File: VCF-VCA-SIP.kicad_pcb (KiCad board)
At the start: 2 copper layers, 40 x 18 mm, 44 parts, among them P1 CONN_10, Q1 BC857BS, U1 LM13700, U2 TL074-, U3 LM13700, U4 LM13700, U5 TL072-

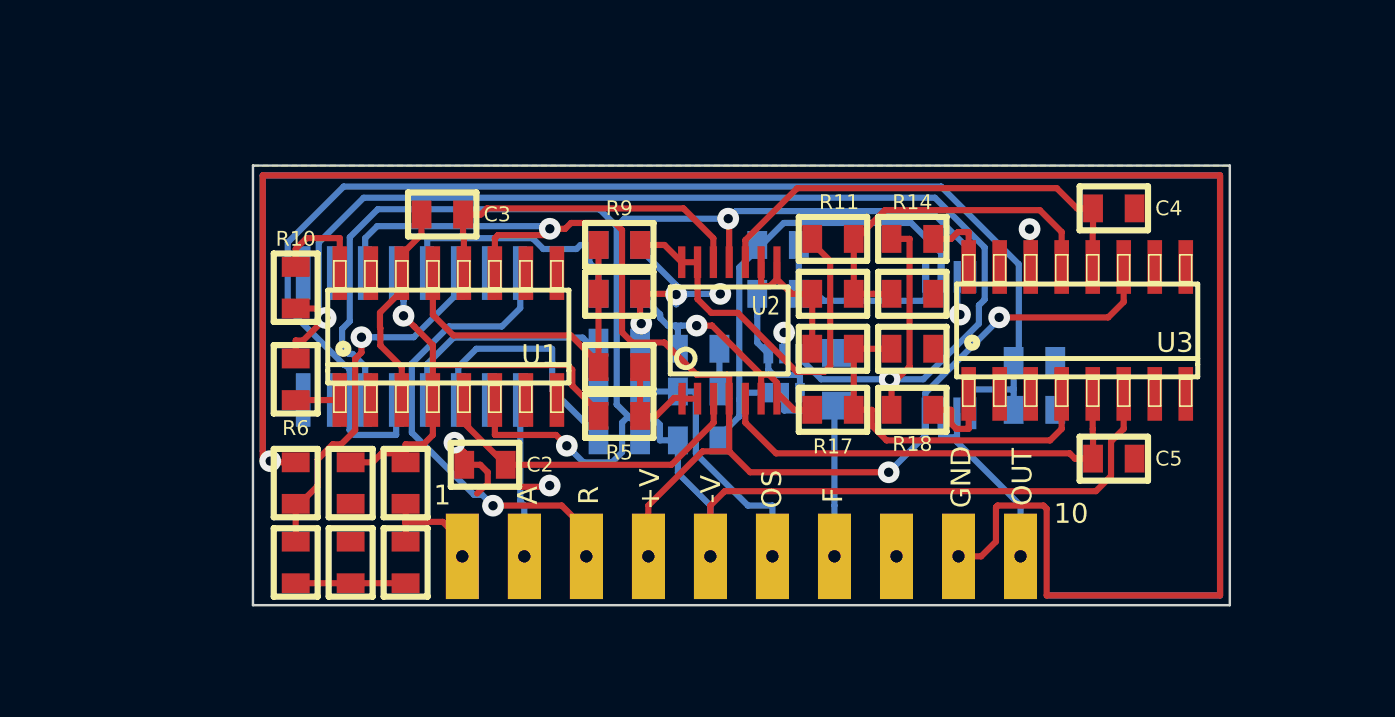
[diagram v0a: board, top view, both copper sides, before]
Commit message: starting to reroute board so trace bewteen LM13700 output in VCA is close to non-inverting input of TL072
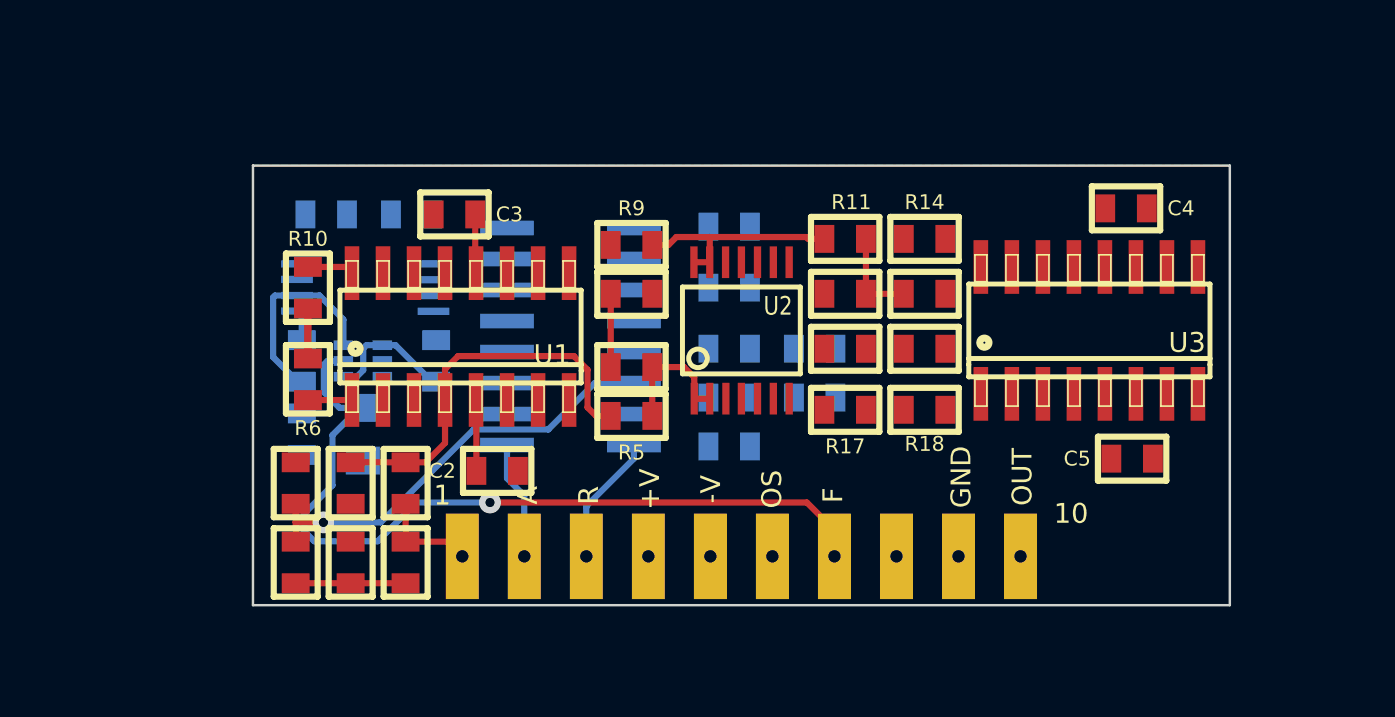
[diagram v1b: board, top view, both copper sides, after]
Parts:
- moved C6 30.1 mm to (101.0, 85.0), turned to 180 degrees
- moved R26 26.2 mm to (104.5, 85.0)
- moved U5 24.1 mm to (102.5, 88.0), turned to 90 degrees
- moved C1 20.1 mm to (100.0, 91.0), turned to 270 degrees
- moved R29 19.6 mm to (102.5, 94.0), turned to 270 degrees
- moved Q1 17.3 mm to (102.5, 91.0), turned to 270 degrees
- moved R1 16.3 mm to (100.0, 94.0), turned to 270 degrees
- moved R2 14.3 mm to (105.5, 91.0), turned to 90 degrees
- moved U4 6.50 mm to (111.0, 90.0), turned to 90 degrees
- moved R30 4.76 mm to (121.0, 92.5)
- moved C7 4.75 mm to (121.0, 90.5)
- moved R22 4.56 mm to (117.5, 85.5)
- moved R20 4.51 mm to (117.5, 88.0)
- moved R23 4.51 mm to (117.5, 92.5)
- moved R24 4.51 mm to (117.5, 90.5)
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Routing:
- net GND: track 188.2 -> 0.00 mm, vias 9 -> 0
- net -VCC: track 84.8 -> 0.00 mm, vias 2 -> 0
- net +VCC: track 57.0 -> 0.00 mm, vias 3 -> 0
- net Iabc: track 56.1 -> 2.05 mm, vias 2 -> 0
- net Net-(C6-Pad1): track 53.1 -> 0.00 mm
- net VCF_CTRL: track 9.15 -> 34.0 mm, vias 0 -> 1
- net Net-(C4-Pad1): track 18.8 -> 0.00 mm
- net Net-(C5-Pad1): track 18.5 -> 0.00 mm
- net Net-(R15-Pad1): track 15.1 -> 0.00 mm
- net RES_CTRL: track 19.5 -> 5.36 mm, vias 1 -> 0
- net Net-(C3-Pad1): track 14.3 -> 2.42 mm
- net VCF_OUT: track 11.7 -> 0.00 mm, vias 1 -> 0
- net Net-(R7-Pad1): track 14.5 -> 3.00 mm
- net Net-(R23-Pad1): track 11.2 -> 0.00 mm
- net Net-(R11-Pad1): track 14.8 -> 3.80 mm
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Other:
- net class POWER added: clearance 0.254, trace_width 0.3048, via_dia 0.889, via_drill 0.381

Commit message: routing
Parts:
- added U6: TL072-, MyModules:TSSOP8-JRL, B.Cu at (133.5, 91.0)
- C1, C2, C3, C4, C5: footprint SM0603-JRL -> MyModules:SM0603-C-JRL
- C6: footprint SM0603-JRL -> MyModules:SM0603-C-JRL; moved to F.Cu
- C7: footprint synth:SM0603-JRL -> MyModules:SM0603-C-JRL; moved to F.Cu
- P1: footprint CONN_10X_0100_SMD_THRUHOLE -> synth:CONN_10X_0100_SMD_THRUHOLE
- Q1: footprint SOT363-JRL -> MyModules:SOT363-JRL
- R1, R11, R12, R13, R15, R16, R17, R19, R2, R21, R27, R28, R3, R4, R5, R7, R8, R9: footprint SM0603-JRL -> MyModules:SM0603-R-JRL
- R10, R14, R18, R6: footprint SM0603-JRL -> MyModules:SM0603-R-JRL; moved to B.Cu
- R20, R22, R23, R24, R25, R26, R30: footprint SM0603-JRL -> MyModules:SM0603-R-JRL; moved to F.Cu
- R29: footprint SM0805-HAND -> MyModules:SM0805-HAND
- U1, U3: footprint SO16-JRL -> MyModules:SO16-JRL
- U2: value TL074- -> TL072-; footprint TSSOP14 -> MyModules:TSSOP8-JRL; moved to B.Cu
- U4: value LM13700 -> TL072-; footprint SO16-JRL -> MyModules:TSSOP8-JRL
- U5: value TL072- -> LM13700; footprint TSSOP8-JRL -> MyModules:SO16-JRL; moved to F.Cu
- moved C6 38.5 mm to (138.5, 93.5), turned to 0 degrees
- moved R26 34.6 mm to (138.5, 91.5)
- moved R29 31.7 mm to (133.0, 85.5), turned to 180 degrees
- moved R27 31.0 mm to (127.5, 85.5), turned to 0 degrees
- moved Q1 30.7 mm to (133.0, 87.5), turned to 90 degrees
- moved U5 30.6 mm to (133.0, 90.0), turned to 270 degrees
- moved R21 29.0 mm to (127.5, 87.5), turned to 180 degrees
- moved R1 28.3 mm to (128.0, 90.0), turned to 0 degrees
- moved C1 28.0 mm to (128.0, 92.0), turned to 180 degrees
- moved R2 24.4 mm to (129.8, 88.0), turned to 180 degrees
- moved R25 22.8 mm to (138.5, 85.5)
- moved C4 22.3 mm to (112.5, 91.5), turned to 180 degrees
- moved R23 21.2 mm to (138.5, 89.5)
- moved R24 21.2 mm to (138.5, 87.5)
- moved R5 16.9 mm to (97.0, 89.5), turned to 0 degrees
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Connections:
- U2 pad 4: +VCC -> -VCC
- U2 pad 5: Net-(C5-Pad1) -> Net-(C3-Pad1)
- U2 pad 6: VCF_OUT -> Net-(R11-Pad2)
- U2 pad 7: VCF_OUT -> Net-(R11-Pad2)
- U2 pad 8: Net-(R13-Pad1) -> +VCC
- U3 pad 1: Net-(R18-Pad1) -> Net-(R14-Pad1)
- U3 pad 12: Net-(C4-Pad1) -> Net-(C5-Pad1)
- U3 pad 13: Net-(R11-Pad1) -> Net-(R15-Pad1)
- U3 pad 16: Net-(R14-Pad1) -> Net-(R18-Pad1)
- U3 pad 4: Net-(R15-Pad1) -> Net-(R11-Pad1)
- U3 pad 5: Net-(C5-Pad1) -> Net-(C4-Pad1)
- U4 pad 1: VCA_CTRL -> Net-(R13-Pad1)
- U4 pad 2: Net-(U4-Pad2) -> Net-(R13-Pad1)
- U4 pad 3: Net-(R25-Pad1) -> Net-(C4-Pad1)
- U4 pad 4: Net-(R23-Pad1) -> -VCC
- U4 pad 5: Net-(C6-Pad1) -> Net-(C5-Pad1)
- U4 pad 6: -VCC -> VCF_OUT
- U4 pad 7: (no net) -> VCF_OUT
- U4 pad 8: (no net) -> +VCC
- U5 pad 1: Net-(C1-Pad1) -> RES_CTRL
- U5 pad 2: Net-(C1-Pad2) -> Net-(U5-Pad2)
- U5 pad 3: GND -> Net-(R21-Pad1)
- U5 pad 4: -VCC -> Net-(R20-Pad1)
- U5 pad 5: Net-(C6-Pad1) -> Net-(R3-Pad2)
- U5 pad 6: VCA_OUT -> -VCC
- U5 pad 7: VCA_OUT -> (no net)
- U5 pad 8: +VCC -> (no net)
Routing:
- net +VCC: track 0.00 -> 59.8 mm, vias 0 -> 3
- net -VCC: track 0.00 -> 53.4 mm, vias 0 -> 3
- net Net-(R19-Pad2): track 4.50 -> 42.4 mm
- net VCA_CTRL: track 4.85 -> 41.0 mm, vias 0 -> 1
- net Iabc: track 2.05 -> 36.8 mm
- net OFFSET: track 0.00 -> 31.2 mm
- net RES_CTRL: track 5.36 -> 35.4 mm, vias 0 -> 1
- net Net-(R13-Pad1): track 0.00 -> 22.1 mm, vias 0 -> 2
- net Net-(R5-Pad1): track 5.40 -> 25.7 mm, vias 0 -> 2
- net VCF_IN: track 4.12 -> 21.2 mm
- net VCA_OUT: track 0.00 -> 15.7 mm
- net VCF_OUT: track 0.00 -> 13.7 mm, vias 0 -> 2
- net Net-(R21-Pad1): track 17.8 -> 4.30 mm, vias 1 -> 0
- net Net-(R3-Pad2): track 16.1 -> 6.61 mm
- net Net-(C6-Pad1): track 0.00 -> 8.26 mm, vias 0 -> 1
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
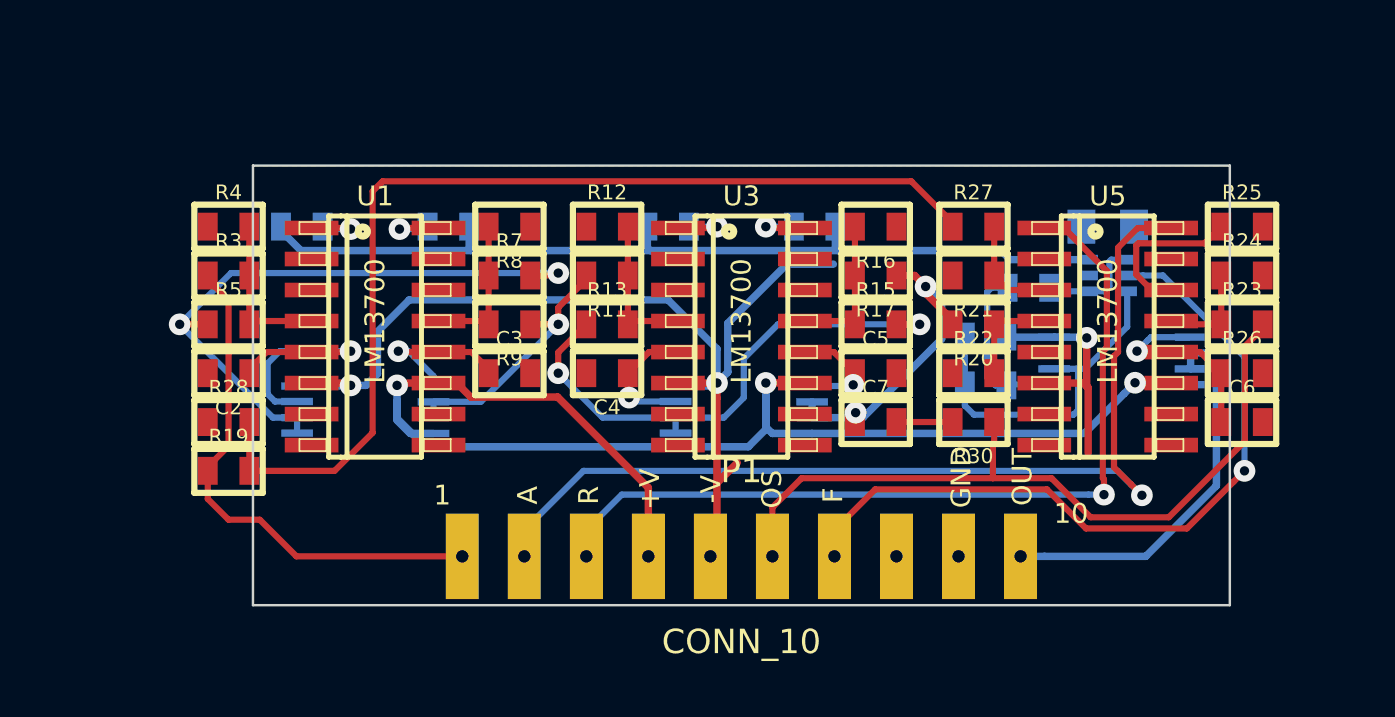
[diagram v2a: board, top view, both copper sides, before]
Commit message: bah. 1 trace left to route. stupid resonance feedback line mistakingly left to last. Don't know if current layout will be feasible because of this
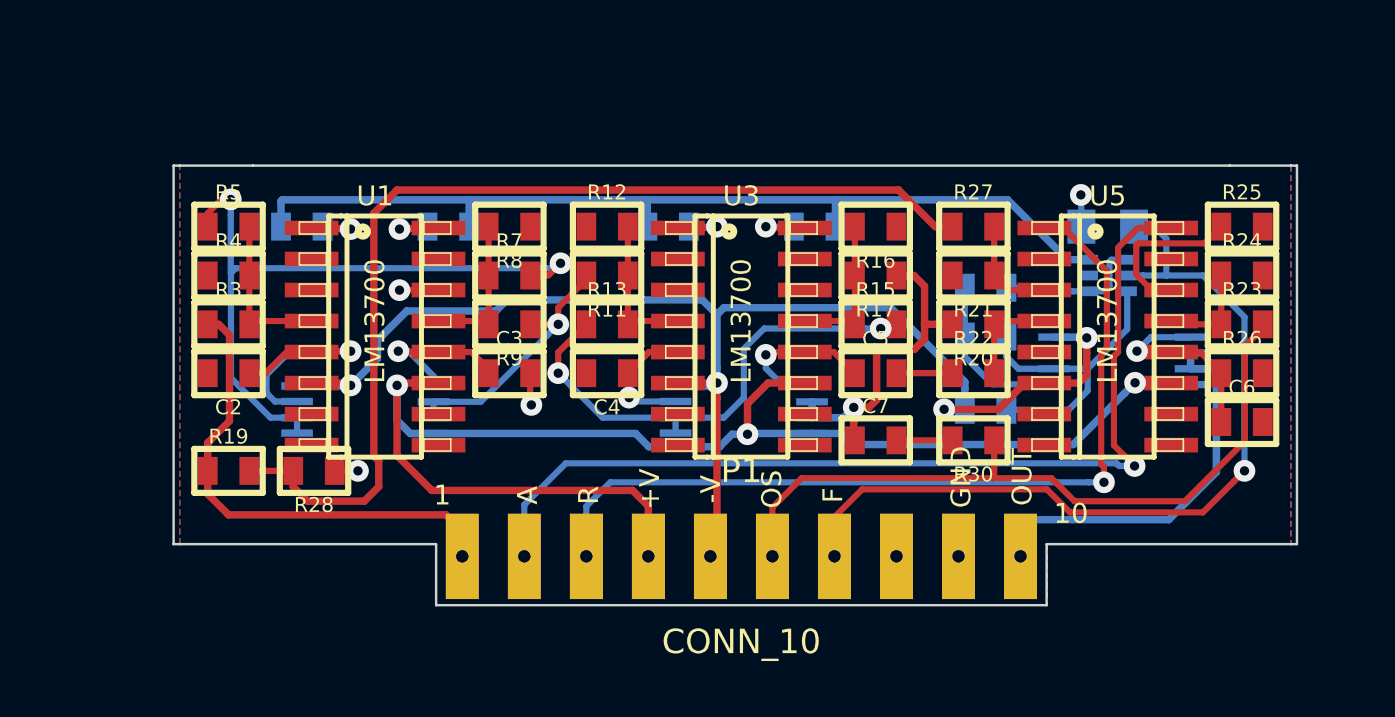
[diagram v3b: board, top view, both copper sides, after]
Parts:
- moved R28 4.03 mm to (100.5, 95.5), turned to 180 degrees
- moved R5 4.00 mm to (97.0, 85.5)
- moved R1 3.00 mm to (128.0, 93.0), turned to 180 degrees
- moved C1 2.00 mm to (128.0, 90.0), turned to 0 degrees
- moved R3 2.00 mm to (97.0, 89.5)
- moved R4 2.00 mm to (97.0, 87.5)
- moved R2 1.75 mm to (128.0, 88.0)
- moved C7 0.75 mm to (123.5, 94.2)
- moved R30 0.75 mm to (127.5, 94.2)
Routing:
- net GND: track 0.00 -> 7.48 mm, vias 0 -> 4
- net VCF_CTRL: track 31.0 -> 34.8 mm
- net -VCC: track 53.4 -> 57.1 mm, vias 3 -> 4
- net Net-(C5-Pad1): track 4.62 -> 7.19 mm
- net Net-(R5-Pad1): track 25.7 -> 28.1 mm
- net Iabc: track 36.8 -> 38.7 mm
- net Net-(Q1-Pad1): track 4.38 -> 6.13 mm
- net Net-(R13-Pad1): track 22.1 -> 20.6 mm
- net Net-(C1-Pad2): track 15.5 -> 14.1 mm
- net VCA_CTRL: track 41.0 -> 39.7 mm
- net VCF_IN: track 21.2 -> 20.2 mm
- net OFFSET: track 31.2 -> 30.2 mm
- net +VCC: track 59.8 -> 60.6 mm
- net VCF_OUT: track 13.7 -> 14.1 mm, vias 2 -> 1
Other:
- board size 40 x 18 mm -> 46 x 18 mm

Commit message: rearrange components and reroute
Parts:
- C2, C3, C4, C5, C7, R11, R12, R13, R15, R16, R17, R19, R28, R3, R4, R5, R7, R8, R9, U1, U3: moved to B.Cu
- R10, R14, R18, R6, U2, U4: moved to F.Cu
- moved R25 27.4 mm to (112.5, 94.0), turned to 180 degrees
- moved C6 27.1 mm to (112.5, 86.0), turned to 180 degrees
- moved R24 26.4 mm to (112.5, 92.0), turned to 180 degrees
- moved R26 26.2 mm to (112.5, 88.0), turned to 180 degrees
- moved R23 26.0 mm to (112.5, 90.0), turned to 180 degrees
- moved C4 24.0 mm to (136.5, 91.5), turned to 0 degrees
- moved R11 24.0 mm to (136.5, 87.5), turned to 0 degrees
- moved R12 24.0 mm to (136.5, 85.5), turned to 180 degrees
- moved R13 24.0 mm to (136.5, 89.5), turned to 180 degrees
- moved R14 19.0 mm to (134.0, 85.5), turned to 0 degrees
- moved R29 17.3 mm to (117.9, 94.0), turned to 0 degrees
- moved U6 15.7 mm to (118.0, 88.5), turned to 270 degrees
- moved Q1 15.7 mm to (118.0, 92.0), turned to 270 degrees
- moved U5 15.0 mm to (118.0, 89.5), turned to 90 degrees
- moved C1 14.1 mm to (114.0, 91.2)
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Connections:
- U6 pad 1: Net-(C1-Pad1) -> VCA_OUT
- U6 pad 2: Net-(C1-Pad2) -> VCA_OUT
- U6 pad 3: GND -> Net-(C6-Pad1)
- U6 pad 5: Net-(C6-Pad1) -> GND
- U6 pad 6: VCA_OUT -> Net-(C1-Pad2)
- U6 pad 7: VCA_OUT -> Net-(C1-Pad1)
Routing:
- net +VCC: track 60.6 -> 0.00 mm, vias 3 -> 0
- net -VCC: track 57.1 -> 0.00 mm, vias 4 -> 0
- net Net-(R19-Pad2): track 42.6 -> 0.00 mm
- net Iabc: track 38.7 -> 0.00 mm
- net OFFSET: track 30.2 -> 0.00 mm
- net VCA_CTRL: track 39.7 -> 10.2 mm, vias 1 -> 0
- net Net-(R5-Pad1): track 28.1 -> 0.00 mm, vias 2 -> 0
- net RES_CTRL: track 35.7 -> 12.5 mm, vias 1 -> 0
- net VCF_CTRL: track 34.8 -> 12.4 mm, vias 1 -> 0
- net Net-(R13-Pad1): track 20.6 -> 0.00 mm, vias 2 -> 0
- net VCF_OUT: track 14.1 -> 0.00 mm, vias 1 -> 0
- net VCF_IN: track 20.2 -> 8.72 mm
- net Net-(C2-Pad1): track 10.9 -> 0.00 mm, vias 1 -> 0
- net Net-(R11-Pad2): track 10.7 -> 0.00 mm, vias 1 -> 0
- net GND: track 7.48 -> 0.00 mm, vias 4 -> 0
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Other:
- board size 46 x 18 mm -> 42 x 18 mm

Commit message: probably going to give up on this layout. What a pain
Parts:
- C2, C3, C4, C5, C7, R28: moved to F.Cu
- R10, R14, R18, R6: moved to B.Cu
- U1, U3, U5: footprint MyModules:SO16-JRL -> MyModules:SOIC16-12-JRL
- moved R20 12.0 mm to (112.0, 86.8), turned to 180 degrees
- moved R21 11.6 mm to (112.0, 90.8), turned to 180 degrees
- moved R27 11.6 mm to (112.0, 92.8), turned to 0 degrees
- moved R22 11.5 mm to (112.0, 88.8), turned to 0 degrees
- moved C6 11.3 mm to (123.8, 85.8), turned to 0 degrees
- moved R23 11.3 mm to (123.8, 89.8), turned to 0 degrees
- moved R24 11.3 mm to (123.8, 91.8), turned to 0 degrees
- moved R25 11.3 mm to (123.8, 93.8), turned to 0 degrees
- moved R26 11.3 mm to (123.8, 87.8), turned to 0 degrees
- moved C2 10.1 mm to (101.5, 87.2), turned to 180 degrees
- moved R28 9.86 mm to (109.0, 92.8)
- moved C4 9.68 mm to (127.6, 87.7), turned to 180 degrees
- moved R8 7.25 mm to (99.5, 92.5)
- moved R30 6.12 mm to (127.6, 89.8)
- moved R12 4.00 mm to (136.5, 89.5)
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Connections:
- U5 pad 1: RES_CTRL -> VCA_CTRL
- U5 pad 12: Net-(C6-Pad1) -> Net-(R3-Pad2)
- U5 pad 13: Net-(R23-Pad1) -> Net-(R20-Pad1)
- U5 pad 14: Net-(R25-Pad1) -> Net-(R21-Pad1)
- U5 pad 16: VCA_CTRL -> RES_CTRL
- U5 pad 3: Net-(R21-Pad1) -> Net-(R25-Pad1)
- U5 pad 4: Net-(R20-Pad1) -> Net-(R23-Pad1)
- U5 pad 5: Net-(R3-Pad2) -> Net-(C6-Pad1)
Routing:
- net -VCC: track 0.00 -> 81.4 mm, vias 0 -> 6
- net +VCC: track 0.00 -> 66.8 mm, vias 0 -> 4
- net Net-(R11-Pad2): track 0.00 -> 58.4 mm, vias 0 -> 1
- net VCF_OUT: track 0.00 -> 43.9 mm, vias 0 -> 1
- net Iabc: track 0.00 -> 38.4 mm
- net Net-(R13-Pad1): track 0.00 -> 19.9 mm, vias 0 -> 2
- net Net-(R5-Pad1): track 0.00 -> 16.3 mm, vias 0 -> 2
- net OFFSET: track 0.00 -> 15.9 mm
- net Net-(R3-Pad2): track 0.00 -> 13.3 mm, vias 0 -> 1
- net Net-(C4-Pad1): track 0.00 -> 12.0 mm, vias 0 -> 1
- net Net-(C2-Pad1): track 0.00 -> 9.91 mm, vias 0 -> 1
- net VCA_CTRL: track 10.2 -> 17.0 mm, vias 0 -> 1
- net Net-(C5-Pad1): track 0.00 -> 6.49 mm, vias 0 -> 1
- net Net-(R7-Pad1): track 0.00 -> 6.20 mm
- net Net-(R15-Pad1): track 0.00 -> 6.11 mm
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
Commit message: still struggling. about to go back to original layout
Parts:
- removed U6: TL072-, MyModules:TSSOP8-JRL
- C6, C7, R20, R22, R23, R24, R25, R26, R30: moved to B.Cu
- R11, R12, R13, R14, R15, R16, R17, R18, R19, R3, R4, R5, R7, R8, R9, U1, U3: moved to F.Cu
- U2: value TL072- -> TL074-; footprint MyModules:TSSOP8-JRL -> Housings_SSOP:TSSOP-14_4.4x5mm_Pitch0.65mm
- U4: value TL072- -> LM13700; footprint MyModules:TSSOP8-JRL -> MyModules:SOIC16-12-JRL; moved to B.Cu
- U5: value LM13700 -> TL072-; footprint MyModules:SOIC16-12-JRL -> MyModules:TSSOP8-JRL; moved to B.Cu
- moved R24 33.5 mm to (90.9, 85.0)
- moved R25 32.6 mm to (91.6, 88.2)
- moved C7 31.1 mm to (96.6, 93.0)
- moved R30 31.1 mm to (96.6, 90.5)
- moved R23 30.9 mm to (92.9, 91.2)
- moved U4 24.0 mm to (107.0, 89.0), turned to 0 degrees
- moved R8 18.5 mm to (116.8, 85.8), turned to 270 degrees
- moved R20 17.8 mm to (96.6, 95.8)
- moved R9 17.3 mm to (116.8, 88.6), turned to 270 degrees
- moved U2 16.3 mm to (120.8, 88.5), turned to 90 degrees
- moved R7 15.4 mm to (114.8, 88.6), turned to 270 degrees
- moved C3 14.9 mm to (114.8, 85.8), turned to 270 degrees
- moved R27 13.9 mm to (100.5, 85.0), turned to 90 degrees
- moved R26 13.5 mm to (110.5, 85.4), turned to 270 degrees
- moved R22 13.3 mm to (100.5, 95.5)
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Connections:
- U1 pad 1: Net-(R6-Pad1) -> Net-(R10-Pad1)
- U1 pad 12: Net-(C3-Pad1) -> Net-(C2-Pad1)
- U1 pad 13: Net-(R7-Pad1) -> Net-(R3-Pad2)
- U1 pad 16: Net-(R10-Pad1) -> Net-(R6-Pad1)
- U1 pad 4: Net-(R3-Pad2) -> Net-(R7-Pad1)
- U1 pad 5: Net-(C2-Pad1) -> Net-(C3-Pad1)
- U2 pad 4: -VCC -> +VCC
- U2 pad 5: Net-(C3-Pad1) -> Net-(C4-Pad1)
- U2 pad 6: Net-(R11-Pad2) -> Net-(R13-Pad1)
- U2 pad 7: Net-(R11-Pad2) -> Net-(R13-Pad1)
- U2 pad 8: +VCC -> VCF_OUT
- U3 pad 1: Net-(R14-Pad1) -> Net-(R18-Pad1)
- U3 pad 12: Net-(C5-Pad1) -> Net-(C4-Pad1)
- U3 pad 13: Net-(R15-Pad1) -> Net-(R11-Pad1)
- U3 pad 16: Net-(R18-Pad1) -> Net-(R14-Pad1)
- U3 pad 4: Net-(R11-Pad1) -> Net-(R15-Pad1)
- U3 pad 5: Net-(C4-Pad1) -> Net-(C5-Pad1)
- U4 pad 1: Net-(R13-Pad1) -> VCA_CTRL
- U4 pad 2: Net-(R13-Pad1) -> Net-(U4-Pad2)
- U4 pad 3: Net-(C4-Pad1) -> Net-(R25-Pad1)
- U4 pad 4: -VCC -> Net-(R23-Pad1)
- U4 pad 5: Net-(C5-Pad1) -> Net-(C6-Pad1)
- U4 pad 6: VCF_OUT -> -VCC
- U5 pad 1: VCA_CTRL -> VCA_OUT
- U5 pad 2: Net-(U5-Pad2) -> VCA_OUT
- U5 pad 3: Net-(R25-Pad1) -> Net-(C6-Pad1)
- U5 pad 4: Net-(R23-Pad1) -> -VCC
- U5 pad 5: Net-(C6-Pad1) -> GND
- U5 pad 6: -VCC -> Net-(C1-Pad2)
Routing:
- net Net-(R11-Pad2): track 58.4 -> 11.6 mm, vias 1 -> 0
- net VCF_OUT: track 43.9 -> 4.37 mm
- net Iabc: track 38.4 -> 0.00 mm
- net +VCC: track 66.8 -> 42.0 mm, vias 4 -> 2
- net -VCC: track 81.4 -> 56.7 mm, vias 6 -> 3
- net VCA_CTRL: track 17.0 -> 0.00 mm, vias 1 -> 0
- net VCA_OUT: track 19.3 -> 2.87 mm
- net OFFSET: track 15.9 -> 0.00 mm
- net Net-(R3-Pad2): track 13.3 -> 26.9 mm
- net Net-(R15-Pad1): track 6.11 -> 19.1 mm
- net Net-(R13-Pad1): track 19.9 -> 7.12 mm, vias 2 -> 0
- net Net-(C2-Pad1): track 9.91 -> 21.9 mm, vias 1 -> 0
- net Net-(C6-Pad1): track 7.41 -> 18.4 mm, vias 1 -> 0
- net Net-(C3-Pad1): track 5.40 -> 16.3 mm, vias 1 -> 0
- net RES_CTRL: track 10.5 -> 0.00 mm
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- removed copper zone on B.Cu, net GND
- removed copper zone on F.Cu, net GND
